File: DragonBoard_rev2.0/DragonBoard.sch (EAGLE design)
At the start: 139 parts, among them IC1 EP4CE15E22C8N, IC2 CP2102, IC3 TPD12S016PWR, J2 RAHHD19TR, X1 PN61729-S

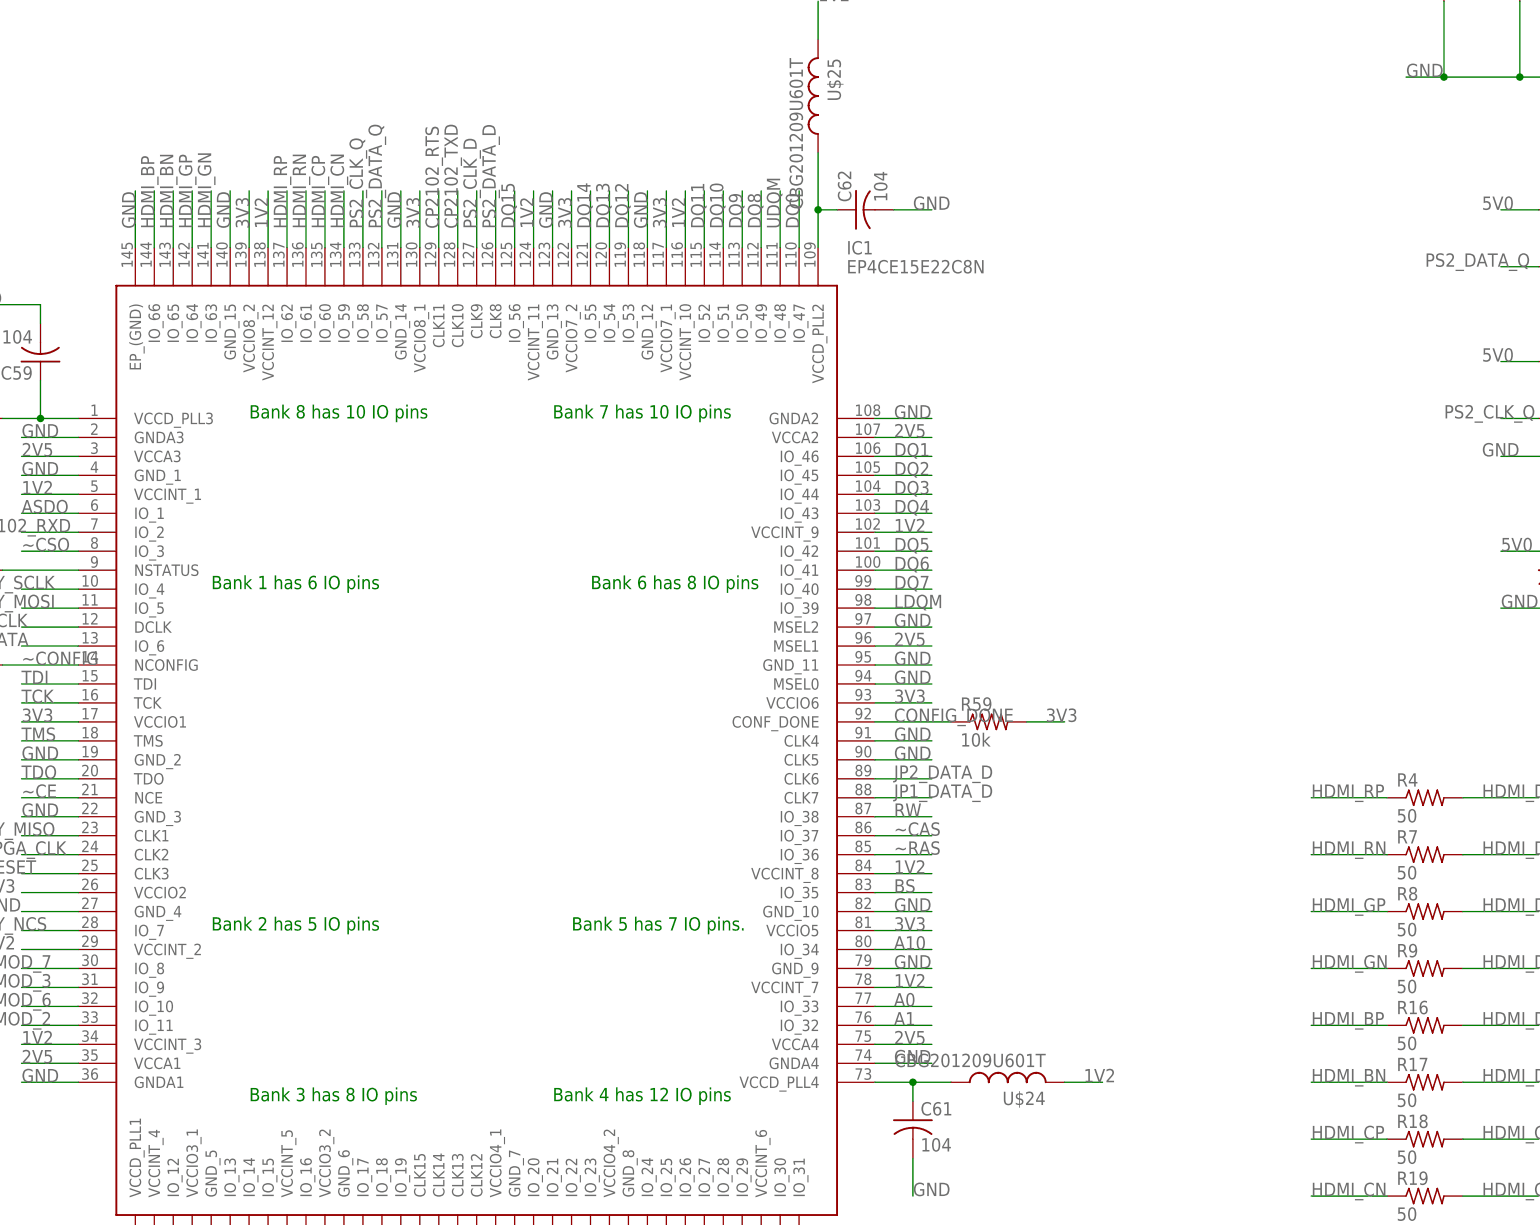
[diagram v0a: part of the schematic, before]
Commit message: fixed HDMI signal names in V2.0, fixed missing I2C resistors in V1.0
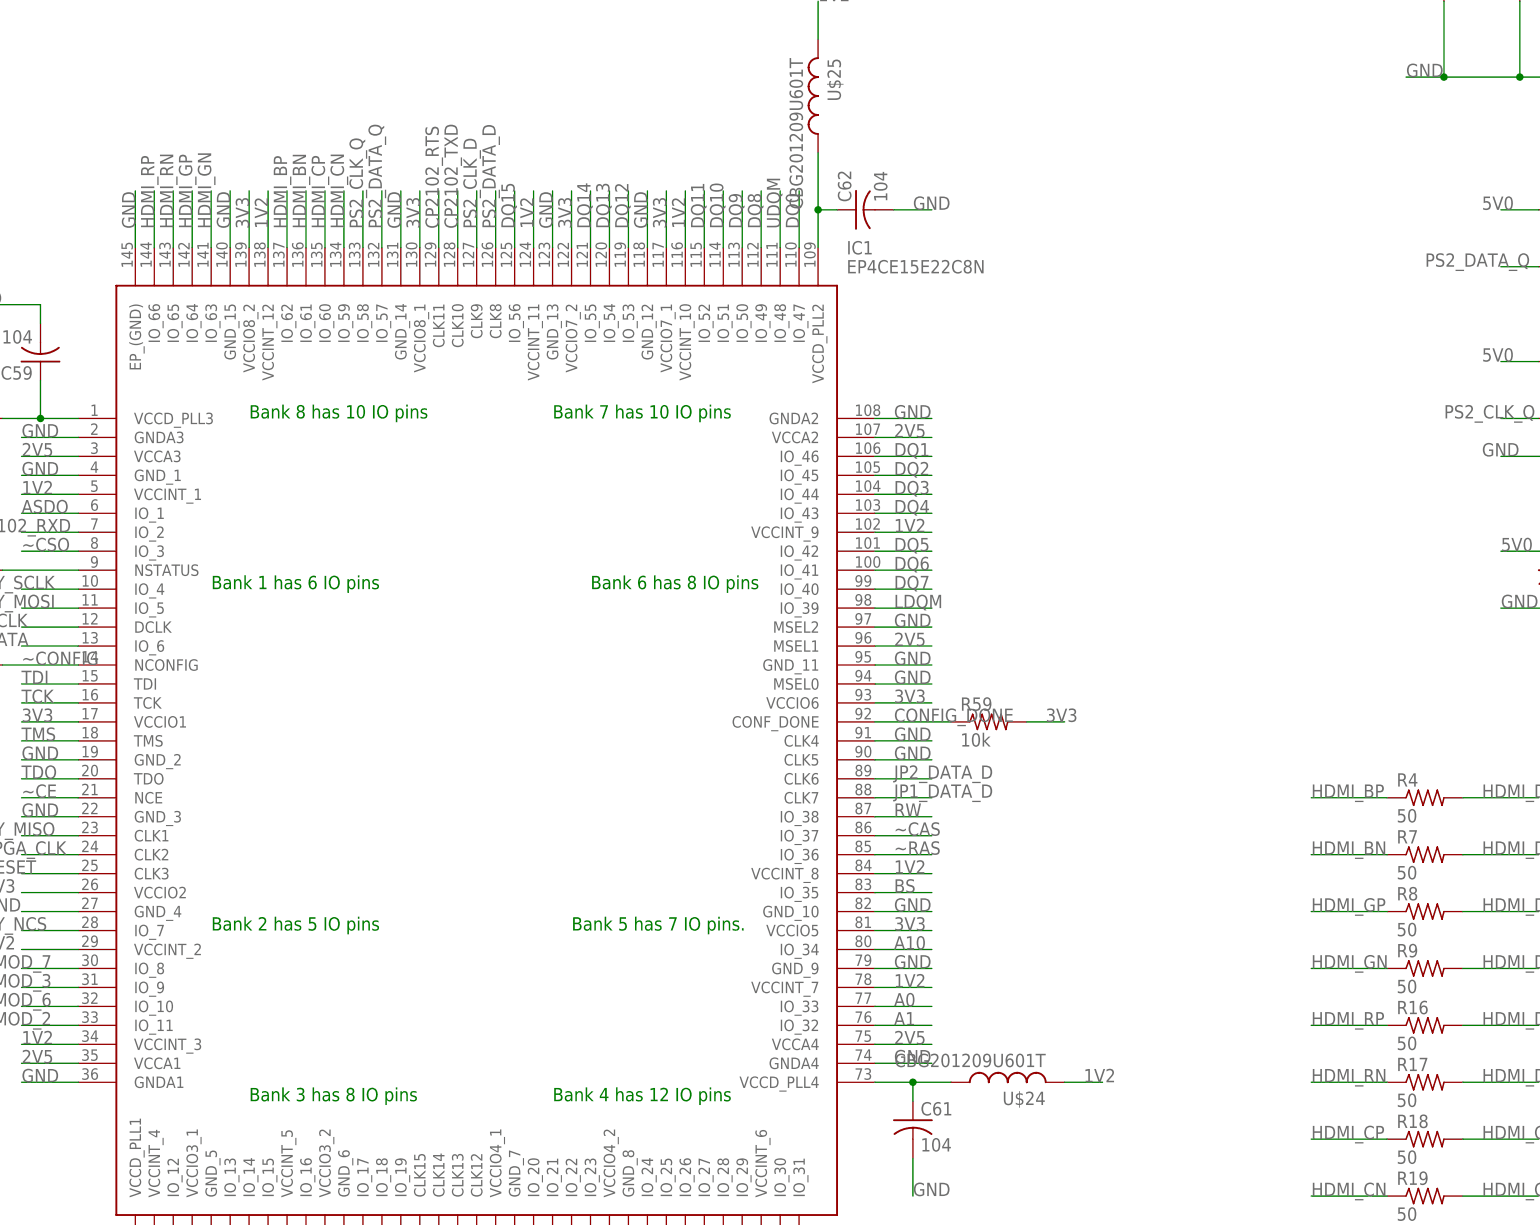
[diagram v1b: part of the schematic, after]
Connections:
- net HDMI_BN: now also IC1.IO_61, R7.1; no longer IC1.IO_65, R17.1
- net HDMI_BP: now also IC1.IO_62, R4.1; no longer IC1.IO_66, R16.1
- net HDMI_RN: now also IC1.IO_65, R17.1; no longer IC1.IO_61, R7.1
- net HDMI_RP: now also IC1.IO_66, R16.1; no longer IC1.IO_62, R4.1
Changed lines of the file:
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@@
 </segment>
 </net>
-<net name="HDMI_RP" class="0">
+<net name="HDMI_BP" class="0">
 <segment>
 <pinref part="R4" gate="G$1" pin="1"/>
@@
 </segment>
 </net>
-<net name="HDMI_RN" class="0">
+<net name="HDMI_BN" class="0">
 <segment>
 <pinref part="R7" gate="G$1" pin="1"/>
@@
 </segment>
 </net>
-<net name="HDMI_BP" class="0">
+<net name="HDMI_RP" class="0">
 <segment>
 <pinref part="R16" gate="G$1" pin="1"/>
@@
 </segment>
 </net>
-<net name="HDMI_BN" class="0">
+<net name="HDMI_RN" class="0">
 <segment>
 <pinref part="R17" gate="G$1" pin="1"/>
